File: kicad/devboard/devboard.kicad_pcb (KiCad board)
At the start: 2 copper layers, 36 parts, among them J1 USB_C_Receptacle, J2 Conn_01x04_Socket, J3 Conn_02x03_Top_Bottom, J4 Conn_02x02_Top_Bottom, U1 LM3940, U2 CH340G, U3 STM32G030K8Tx, Y1 12 MHz, Y2 8 MHz

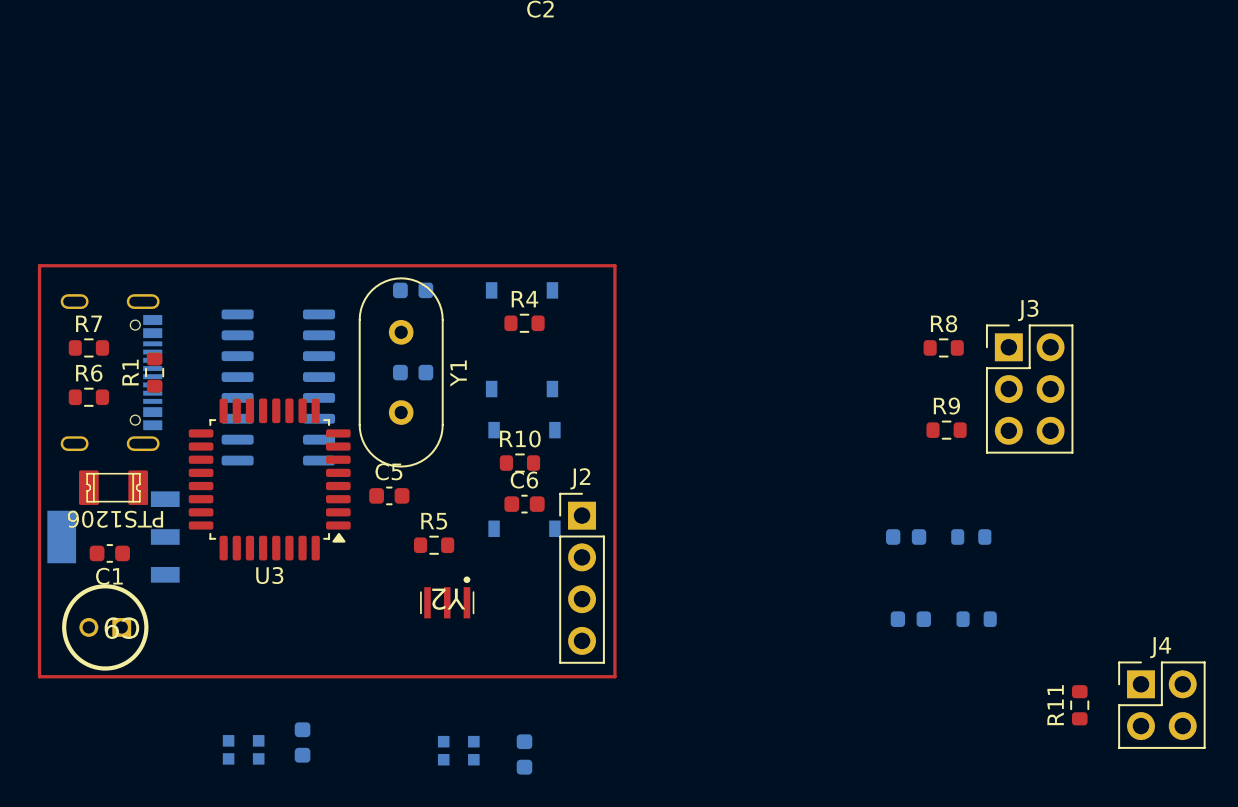
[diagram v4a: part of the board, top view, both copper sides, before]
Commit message: Move connectors to the top
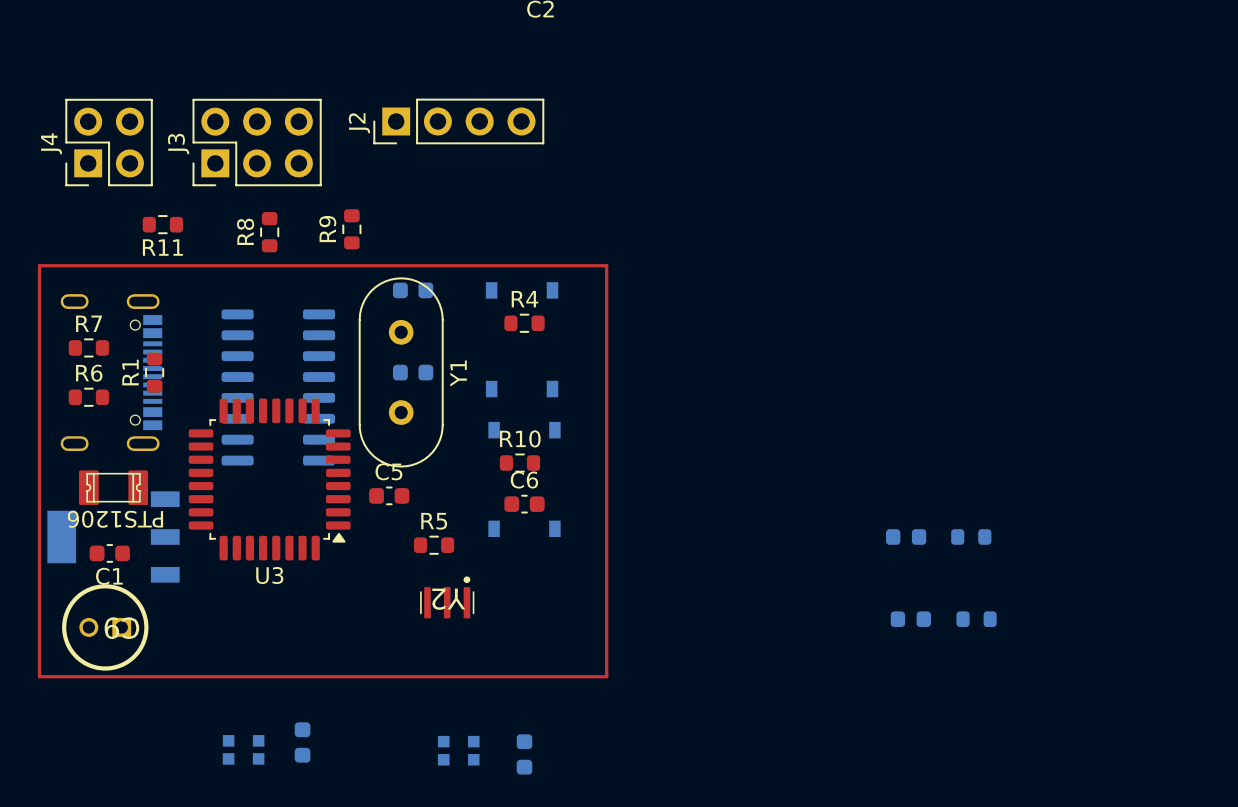
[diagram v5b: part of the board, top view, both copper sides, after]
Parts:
- moved J4 71.4 mm to (104.0, 42.8), turned to 90 degrees
- moved R11 63.0 mm to (108.5, 46.5), turned to 180 degrees
- moved J3 49.5 mm to (111.7, 42.8), turned to 90 degrees
- moved R8 41.6 mm to (115.0, 47.0), turned to 90 degrees
- moved R9 38.2 mm to (120.0, 46.8), turned to 90 degrees
- moved J2 26.5 mm to (122.7, 40.2), turned to 90 degrees

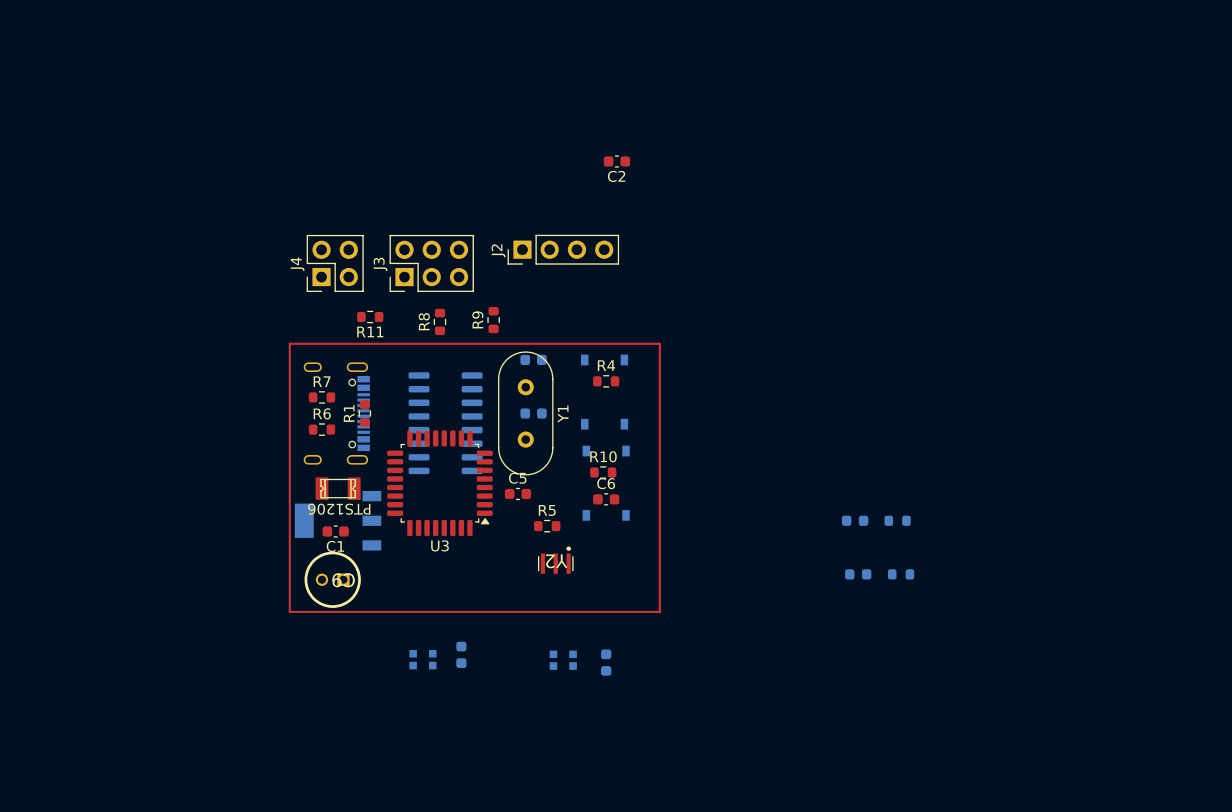
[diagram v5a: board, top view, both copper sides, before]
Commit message: Added 3pad resistor comment, and spread the board out
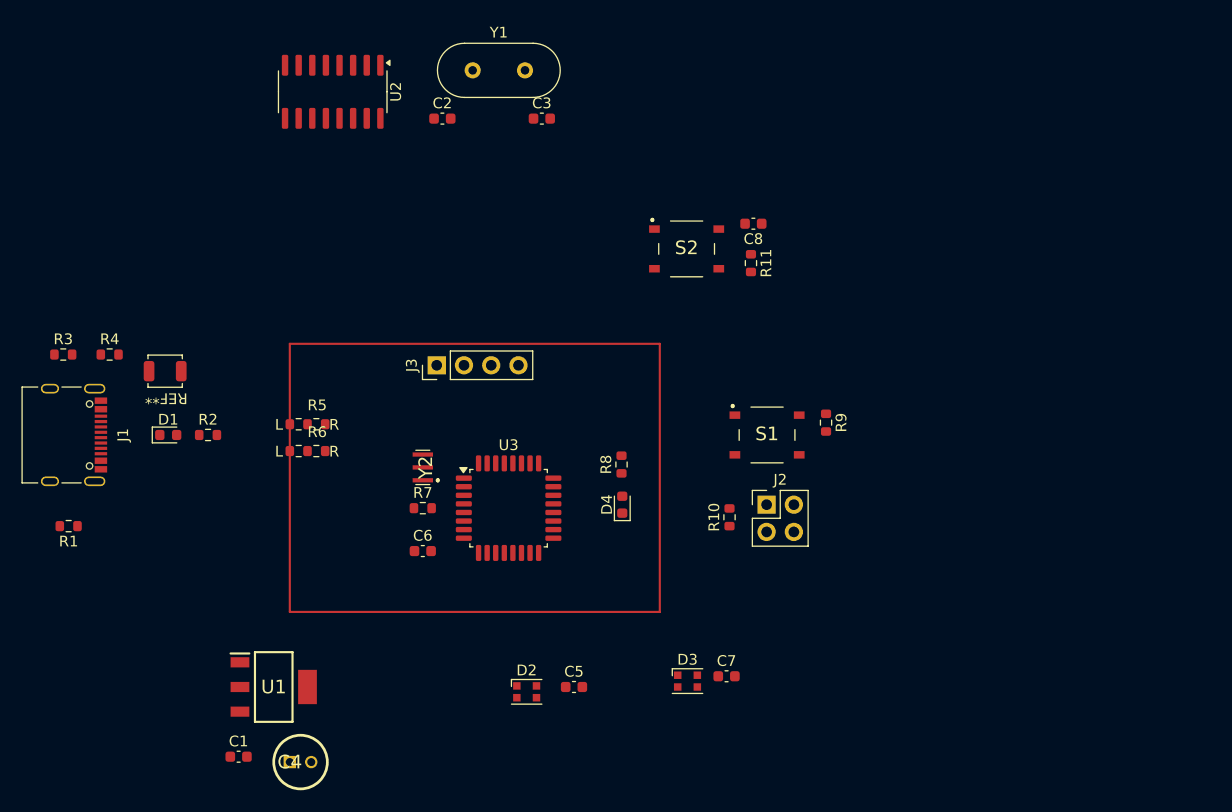
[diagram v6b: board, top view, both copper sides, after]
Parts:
- removed C9: EEU-FR1V330, mesonlib:EEU-FR1330
- removed J4: Conn_02x02_Top_Bottom, Connector_PinHeader_2.54mm:PinHeader_2x02_P2.54mm_Vertical
- C2: value 33 uF -> 22 pF
- C3, C7, D1, D2, D3, D4, J1, R2, S1, S2, U1, U2: moved to F.Cu
- C4: value 22 pF -> EEU-FR1V330; footprint Capacitor_SMD:C_0603_1608Metric -> mesonlib:EEU-FR1330; moved to F.Cu
- C6: value 0.1 uF -> 100 nF
- C8: value 100 nF -> 0.1 uF; moved to F.Cu
- J2: value Conn_01x04_Socket -> Conn_02x02_Top_Bottom; footprint Connector_PinHeader_2.54mm:PinHeader_1x04_P2.54mm_Vertical -> Connector_PinHeader_2.54mm:PinHeader_2x02_P2.54mm_Vertical
- J3: value Conn_02x03_Top_Bottom -> Conn_01x04_Socket; footprint Connector_PinHeader_2.54mm:PinHeader_2x03_P2.54mm_Vertical -> Connector_PinHeader_2.54mm:PinHeader_1x04_P2.54mm_Vertical
- R3: value 470 -> 5k1; moved to F.Cu
- R4: value 10k -> 5k1
- R5: value 603 -> 1k; footprint Resistor_SMD:R_0603_1608Metric -> mesonlib:resistor_3pad_switch_0603
- R6: value 5k1 -> 1k; footprint Resistor_SMD:R_0603_1608Metric -> mesonlib:resistor_3pad_switch_0603
- R7: value 5k1 -> 603
- R8: value 1k -> 470
- R9: value 1k -> 10k
- moved R3 80.8 mm to (79.9, 50.0)
- moved R2 64.8 mm to (93.4, 57.5)
- moved D1 64.5 mm to (89.7, 57.5), turned to 0 degrees
- moved C8 48.6 mm to (144.2, 37.8), turned to 180 degrees
- moved R4 46.4 mm to (84.2, 50.0)
- moved C4 39.7 mm to (101.0, 88.0)
- moved R11 35.9 mm to (144.0, 41.5), turned to -90 degrees
- moved J2 32.9 mm to (145.5, 64.0), turned to 0 degrees
- moved U2 32.6 mm to (105.0, 25.5), turned to -90 degrees
- moved R9 32.4 mm to (151.0, 56.4), turned to -90 degrees
- moved Y1 30.0 mm to (118.0, 23.5), turned to 0 degrees
- moved R1 29.6 mm to (80.4, 66.0), turned to 180 degrees
- moved R5 25.8 mm to (101.0, 56.5)
- moved D3 24.8 mm to (138.1, 80.5), turned to 0 degrees
- moved J1 24.6 mm to (80.9, 57.5), turned to -90 degrees
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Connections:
- C2 pad 1: +3.3V -> Net-(U2-XI)
- C3 pad 1: Net-(U2-XI) -> Net-(U2-XO)
- C4 pad 1: Net-(U2-XO) -> +3.3V
- C5 pad 1: +3.3V -> +5V
- C6 pad 1: /RESET -> +3.3V
- C8 pad 1: +5V -> /RESET
- J2 pad 1: +5V -> /SWDIO
- J2 pad 2: /I2C1_SDA -> /SWCLK/BOOT
- J2 pad 3: /I2C1_SCL -> +3.3V
- J3 pad 1: /TX-M -> +5V
- J3 pad 2: /TX-U -> /I2C1_SDA
- J3 pad 3: /RX-M -> /I2C1_SCL
- J3 pad 4: /TX-M -> GND
- R10 pad 2: /RESET -> /SWDIO
- R11 pad 2: /SWDIO -> /RESET
- R3 pad 1: Net-(D4-K) -> Net-(J1-CC1)
- R4 pad 1: /SWCLK/BOOT -> Net-(J1-CC2)
- R5 pad 1: Net-(U3-PC15) -> /TX-M
- R5 pad 2: Net-(R5-Pad2) -> /TX-U
- R6 pad 1: Net-(J1-CC1) -> /TX-M
- R6 pad 2: GND -> /RX-U
- R7 pad 1: Net-(J1-CC2) -> Net-(U3-PC15)
- R7 pad 2: GND -> Net-(R7-Pad2)
- R8 pad 1: /TX-U -> Net-(D4-K)
- R8 pad 2: Net-(U2-TXD) -> GND
- R9 pad 1: Net-(U2-RXD) -> /SWCLK/BOOT
- R9 pad 2: /RX-U -> GND
- U2 pad 2: Net-(U2-TXD) -> /TX-U
- U2 pad 3: Net-(U2-RXD) -> /RX-U
- Y2 pad 1: Net-(R5-Pad2) -> Net-(R7-Pad2)

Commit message: Placed components within shape
it's messy but it fits
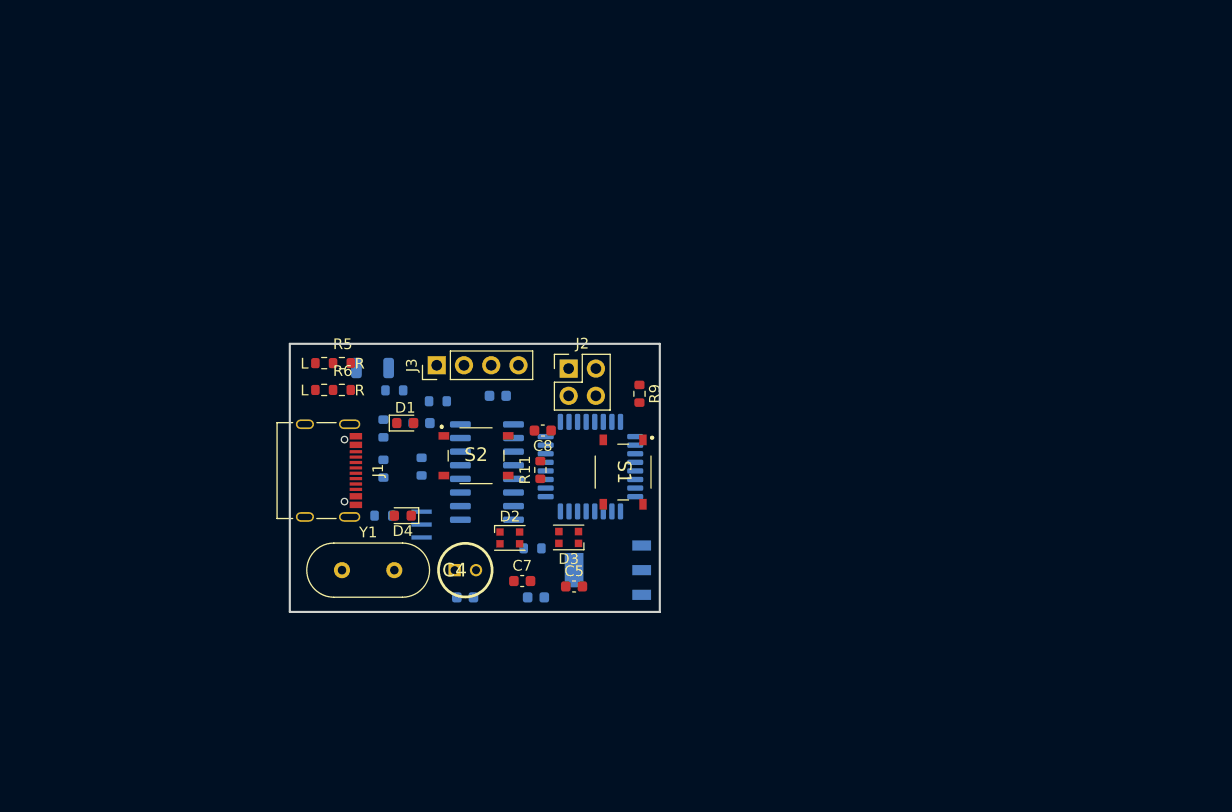
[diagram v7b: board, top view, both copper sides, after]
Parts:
- C1, C2, C3, C6, R1, R10, R2, R3, R4, R7, R8, TH1, U1, U2, U3, Y2: moved to B.Cu
- moved Y1 48.2 mm to (105.9, 70.1)
- moved U2 38.3 mm to (119.4, 61.0), turned to 0 degrees
- moved U1 33.0 mm to (130.7, 70.1), turned to 180 degrees
- moved C1 31.5 mm to (124.0, 72.6), turned to 180 degrees
- moved R3 30.6 mm to (109.7, 56.9), turned to 90 degrees
- moved C3 30.5 mm to (113.3, 56.4), turned to 180 degrees
- moved R1 29.4 mm to (109.7, 65.0)
- moved R4 27.7 mm to (109.7, 60.6), turned to -90 degrees
- moved C8 27.5 mm to (124.6, 57.1)
- moved R11 27.5 mm to (124.4, 60.8), turned to 90 degrees
- moved S2 27.5 mm to (118.4, 59.4)
- moved C2 26.4 mm to (120.4, 53.8)
- moved J1 24.0 mm to (104.6, 60.8)
- moved C4 23.6 mm to (116.4, 70.1)
- moved J2 22.4 mm to (127.0, 51.3)
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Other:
- board outline added: 34.5 x 25 mm
- board text added: "All LEDs, switches (includes R5/6), and through components go on F. Cu"
- board text added: "Everything else goes on B. Cu"
- board text added: "F. Cu is defined as {dblquote}top{dblquote} side of board"

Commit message: started wiring
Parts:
- moved C1 1.27 mm to (122.7, 72.8)
- moved R9 1.03 mm to (132.6, 53.8)
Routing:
- net GND: track 0.00 -> 26.6 mm, vias 0 -> 1
- net +3.3V: track 0.00 -> 22.0 mm, vias 0 -> 1
- net +5V: track 0.00 -> 20.1 mm, vias 0 -> 3
- net /SWCLK/BOOT: track 0.00 -> 16.8 mm
